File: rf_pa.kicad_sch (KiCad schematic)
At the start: 42 parts, among them Q1 BSS138, Q2 NP100P04PDG, U1 LM317_SOT-223, U2 LT1013DIDR, U3 TL431, U4 RA60H3847H1

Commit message: Add files via upload
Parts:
- added C9: 100u/50V, Capacitor_SMD:CP_Elec_8x10.5, symbol Device:C_Polarized_Small
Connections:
- net GND: now also C9.2
- net RF_PA_VDD: now also C9.1
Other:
- moved on the sheet: R2
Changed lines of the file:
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@@
+    (stroke (width 0) (type default))
+  )
+  (wire (pts (xy 309.88 204.47) (xy 309.88 207.01))
     (stroke (width 0) (type default))
   )
@@
     (stroke (width 0) (type default))
   )
+  (wire (pts (xy 309.88 195.58) (xy 309.88 199.39))
+    (stroke (width 0) (type default))
+  )
   (wire (pts (xy 184.15 116.84) (xy 184.15 114.3))
     (stroke (width 0) (type default))
@@
     (stroke (width 0) (type default))
   )
-  (wire (pts (xy 278.13 200.66) (xy 278.13 205.74))
+  (wire (pts (xy 278.13 200.66) (xy 278.13 207.01))
     (stroke (width 0) (type default))
   )
@@
     (stroke (width 0) (type default))
   )
-  (wire (pts (xy 266.7 195.58) (xy 266.7 198.12))
+  (wire (pts (xy 266.7 195.58) (xy 266.7 199.39))
     (stroke (width 0) (type default))
   )
@@
     (stroke (width 0) (type default))
   )
-  (wire (pts (xy 266.7 203.2) (xy 266.7 205.74))
+  (wire (pts (xy 266.7 204.47) (xy 266.7 207.01))
     (stroke (width 0) (type default))
   )
@@
     )
   )
-  (symbol (lib_id "power:GND") (at 266.7 205.74 0) (unit 1)
-    (in_bom yes) (on_board yes) (dnp no) (fields_autoplaced)
-    (property "Reference" "#PWR015" (at 266.7 212.09 0)
-      (effects (font (size 1.27 1.27)) hide)
-    )
-    (property "Value" "GND" (at 266.7 209.8731 0)
-      (effects (font (size 1.27 1.27)))
-    )
-    (property "Footprint" "" (at 266.7 205.74 0)
-      (effects (font (size 1.27 1.27)) hide)
-    )
-    (property "Datasheet" "" (at 266.7 205.74 0)
+  (symbol (lib_id "power:GND") (at 266.7 207.01 0) (unit 1)
+    (in_bom yes) (on_board yes) (dnp no) (fields_autoplaced)
+    (property "Reference" "#PWR015" (at 266.7 213.36 0)
+      (effects (font (size 1.27 1.27)) hide)
+    )
+    (property "Value" "GND" (at 266.7 211.1431 0)
+      (effects (font (size 1.27 1.27)))
+    )
+    (property "Footprint" "" (at 266.7 207.01 0)
+      (effects (font (size 1.27 1.27)) hide)
+    )
+    (property "Datasheet" "" (at 266.7 207.01 0)
       (effects (font (size 1.27 1.27)) hide)
     )
@@
     )
   )
-  (symbol (lib_id "Device:R_Small") (at 266.7 200.66 180) (unit 1)
+  (symbol (lib_id "Device:R_Small") (at 266.7 201.93 180) (unit 1)
     (in_bom yes) (on_board yes) (dnp no)
-    (property "Reference" "R2" (at 270.51 199.39 0)
-      (effects (font (size 1.27 1.27)))
-    )
-    (property "Value" "10k" (at 270.51 201.93 0)
-      (effects (font (size 1.27 1.27)))
-    )
-    (property "Footprint" "Resistor_SMD:R_0603_1608Metric" (at 266.7 200.66 0)
-      (effects (font (size 1.27 1.27)) hide)
-    )
-    (property "Datasheet" "~" (at 266.7 200.66 0)
-      (effects (font (size 1.27 1.27)) hide)
-    )
-    (property "PN" "" (at 266.7 200.66 0)
+    (property "Reference" "R2" (at 270.51 200.66 0)
+      (effects (font (size 1.27 1.27)))
+    )
+    (property "Value" "10k" (at 270.51 203.2 0)
+      (effects (font (size 1.27 1.27)))
+    )
+    (property "Footprint" "Resistor_SMD:R_0603_1608Metric" (at 266.7 201.93 0)
+      (effects (font (size 1.27 1.27)) hide)
+    )
+    (property "Datasheet" "~" (at 266.7 201.93 0)
+      (effects (font (size 1.27 1.27)) hide)
+    )
+    (property "PN" "" (at 266.7 201.93 0)
       (effects (font (size 1.27 1.27)) hide)
     )
@@
     )
   )
-  (symbol (lib_id "power:GND") (at 278.13 205.74 0) (unit 1)
-    (in_bom yes) (on_board yes) (dnp no) (fields_autoplaced)
-    (property "Reference" "#PWR016" (at 278.13 212.09 0)
-      (effects (font (size 1.27 1.27)) hide)
-    )
-    (property "Value" "GND" (at 278.13 209.8731 0)
-      (effects (font (size 1.27 1.27)))
-    )
-    (property "Footprint" "" (at 278.13 205.74 0)
-      (effects (font (size 1.27 1.27)) hide)
-    )
-    (property "Datasheet" "" (at 278.13 205.74 0)
+  (symbol (lib_id "power:GND") (at 278.13 207.01 0) (unit 1)
+    (in_bom yes) (on_board yes) (dnp no) (fields_autoplaced)
+    (property "Reference" "#PWR016" (at 278.13 213.36 0)
+      (effects (font (size 1.27 1.27)) hide)
+    )
+    (property "Value" "GND" (at 278.13 211.1431 0)
+      (effects (font (size 1.27 1.27)))
+    )
+    (property "Footprint" "" (at 278.13 207.01 0)
+      (effects (font (size 1.27 1.27)) hide)
+    )
+    (property "Datasheet" "" (at 278.13 207.01 0)
       (effects (font (size 1.27 1.27)) hide)
     )
@@
         (path "/4c42207c-9e6b-42da-ad38-da126b892014/7ebe248e-d508-4395-8ad3-4ea02a49e591"
           (reference "U1") (unit 1)
+        )
+      )
+    )
+  )
+  (symbol (lib_id "power:GND") (at 309.88 207.01 0) (unit 1)
+    (in_bom yes) (on_board yes) (dnp no) (fields_autoplaced)
+    (property "Reference" "#PWR018" (at 309.88 213.36 0)
+      (effects (font (size 1.27 1.27)) hide)
+    )
+    (property "Value" "GND" (at 309.88 211.1431 0)
+      (effects (font (size 1.27 1.27)))
+    )
+    (property "Footprint" "" (at 309.88 207.01 0)
+      (effects (font (size 1.27 1.27)) hide)
+    )
+    (property "Datasheet" "" (at 309.88 207.01 0)
+      (effects (font (size 1.27 1.27)) hide)
+    )
+    (pin "1")
+    (instances
+      (project "m17-rru-rf"
+        (path "/4c42207c-9e6b-42da-ad38-da126b892014/7ebe248e-d508-4395-8ad3-4ea02a49e591"
+          (reference "#PWR018") (unit 1)
         )
       )
@@
         )
       )
+    )
+  )
+  (symbol (lib_id "Device:C_Polarized_Small") (at 309.88 201.93 0) (unit 1)
+    (in_bom yes) (on_board yes) (dnp no) (fields_autoplaced)
+    (property "Reference" "C9" (at 312.039 200.1718 0)
+      (effects (font (size 1.27 1.27)) (justify left))
+    )
+    (property "Value" "100u/50V" (at 312.039 202.596 0)
+      (effects (font (size 1.27 1.27)) (justify left))
+    )
+    (property "Footprint" "Capacitor_SMD:CP_Elec_8x10.5" (at 309.88 201.93 0)
+      (effects (font (size 1.27 1.27)) hide)
+    )
+    (property "Datasheet" "~" (at 309.88 201.93 0)
+      (effects (font (size 1.27 1.27)) hide)
+    )
+    (property "PN" "50SEV100M8X10.5" (at 309.88 201.93 0)
+      (effects (font (size 1.27 1.27)) hide)
+    )
+    (pin "1")
+    (pin "2")
+    (instances
+      (project "m17-rru-rf"
+        (path "/4c42207c-9e6b-42da-ad38-da126b892014/7ebe248e-d508-4395-8ad3-4ea02a49e591"
+          (reference "C9") (unit 1)
+        )
+      )

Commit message: Add files via upload
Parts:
- added Q1: BSS138, Package_TO_SOT_SMD:SOT-23, symbol Transistor_FET:BSS138
- added R2: 100k, Resistor_SMD:R_0603_1608Metric, symbol Device:R_Small
- added R2: 100R, Resistor_SMD:R_0603_1608Metric, symbol Device:R_Small
- added R2: 10k, Resistor_SMD:R_0603_1608Metric, symbol Device:R_Small
- added TP5: ~, TestPoint:TestPoint_Pad_D1.5mm, symbol Connector:TestPoint_Probe
- Q2: renamed from Q1; PN (none) -> BSS138P,215
- R2: value 47k -> 12k
- renumbered Q2 to Q3, TP5 to TP6, TP6 to TP7
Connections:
- net at Q2.1 (G), R2.2, R2.2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: now also R2.1
- net at Q3.1 (G), R2.1, TP7.1: now also Q1.3 (D); no longer Q2.3 (D)
- net PA_EN renamed PA_EN_B
- new net: Q1.2 (S), Q2.3 (D), R2.1, R2.2
- new net: Q1.1 (G), R2.2, R2.2, TP5.1
- new net PA_EN_A: R2.1
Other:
- moved on the sheet: C9, D3, D4, Q2, Q3, R2, TP6, TP7

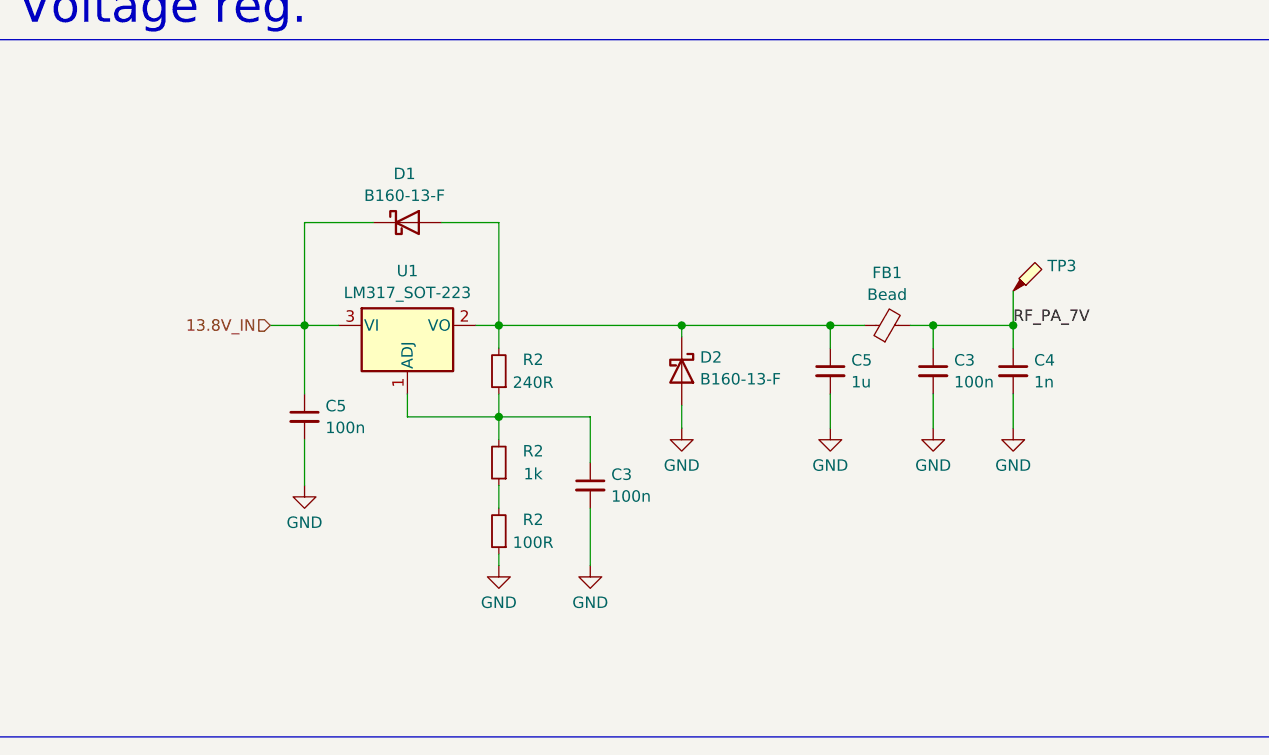
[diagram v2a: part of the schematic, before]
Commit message: LM317 protection diode location update
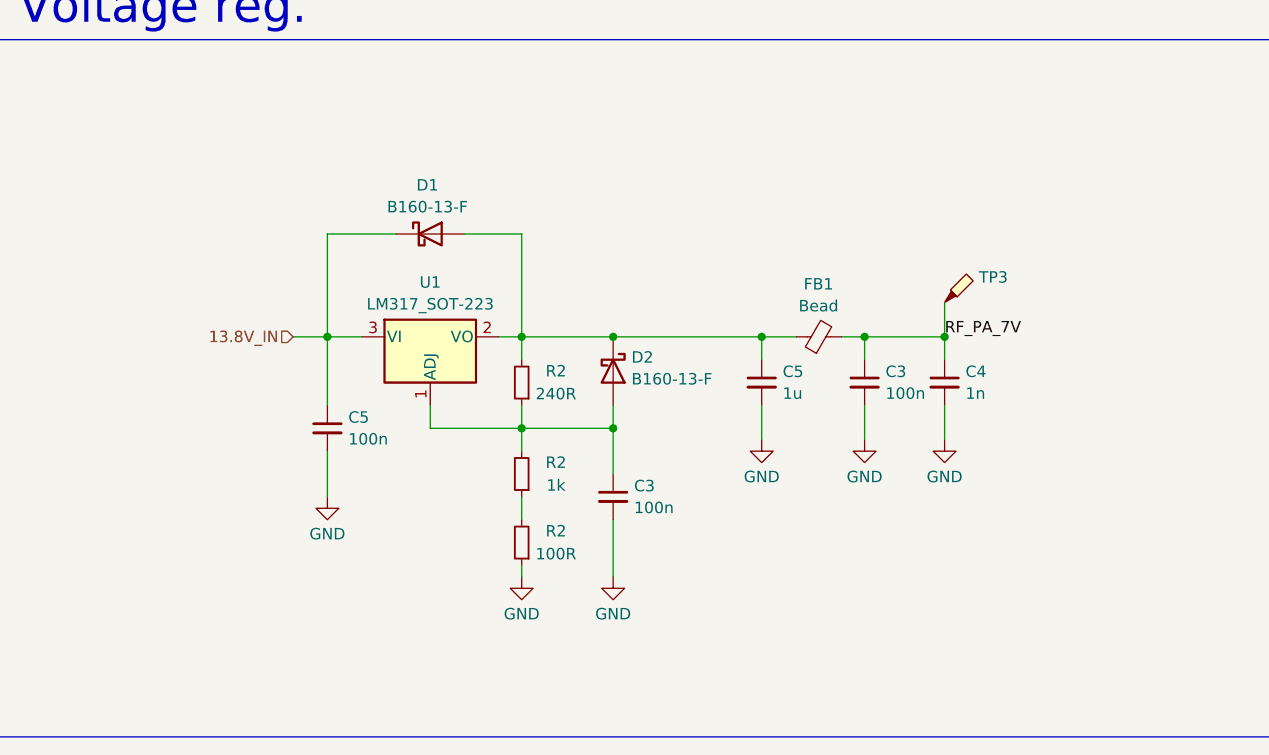
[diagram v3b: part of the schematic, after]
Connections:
- net GND: no longer D2.2 (A)
- net at C3.1, R2.1, R2.2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: now also D2.2 (A)
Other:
- moved on the sheet: C3, C4, C5, D1, D2, FB1, R2, TP3, U1

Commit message: partial PN update
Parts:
- added C3: 3n9, Capacitor_SMD:C_0603_1608Metric, symbol Device:C_Small
- added TP1, TP2: ~, TestPoint:TestPoint_Pad_D1.5mm, symbol Connector:TestPoint_Probe
- C3, C5: PN (none) -> C0603C104M5RAC7411
- C3: PN (none) -> GCM1885C1H392JA16J
- C4: PN (none) -> C0603C102J5GAC7411
- C5: PN (none) -> CL10B105KB8NQNC
- renumbered C9 to C10, TP1 to TP3, TP2 to TP4, TP3 to TP5, TP4 to TP6, TP5 to TP7, TP6 to TP8, TP7 to TP9
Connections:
- net FWD_SENSE_IN: now also TP1.1
- net at R2.1, R2.2, R2.2: now also TP2.1
- net at R2.1, R2.1, U2.4 (2IN-): now also C3.2
- net at R2.2, U2.5 (2OUT): now also C3.1
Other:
- moved on the sheet: D2

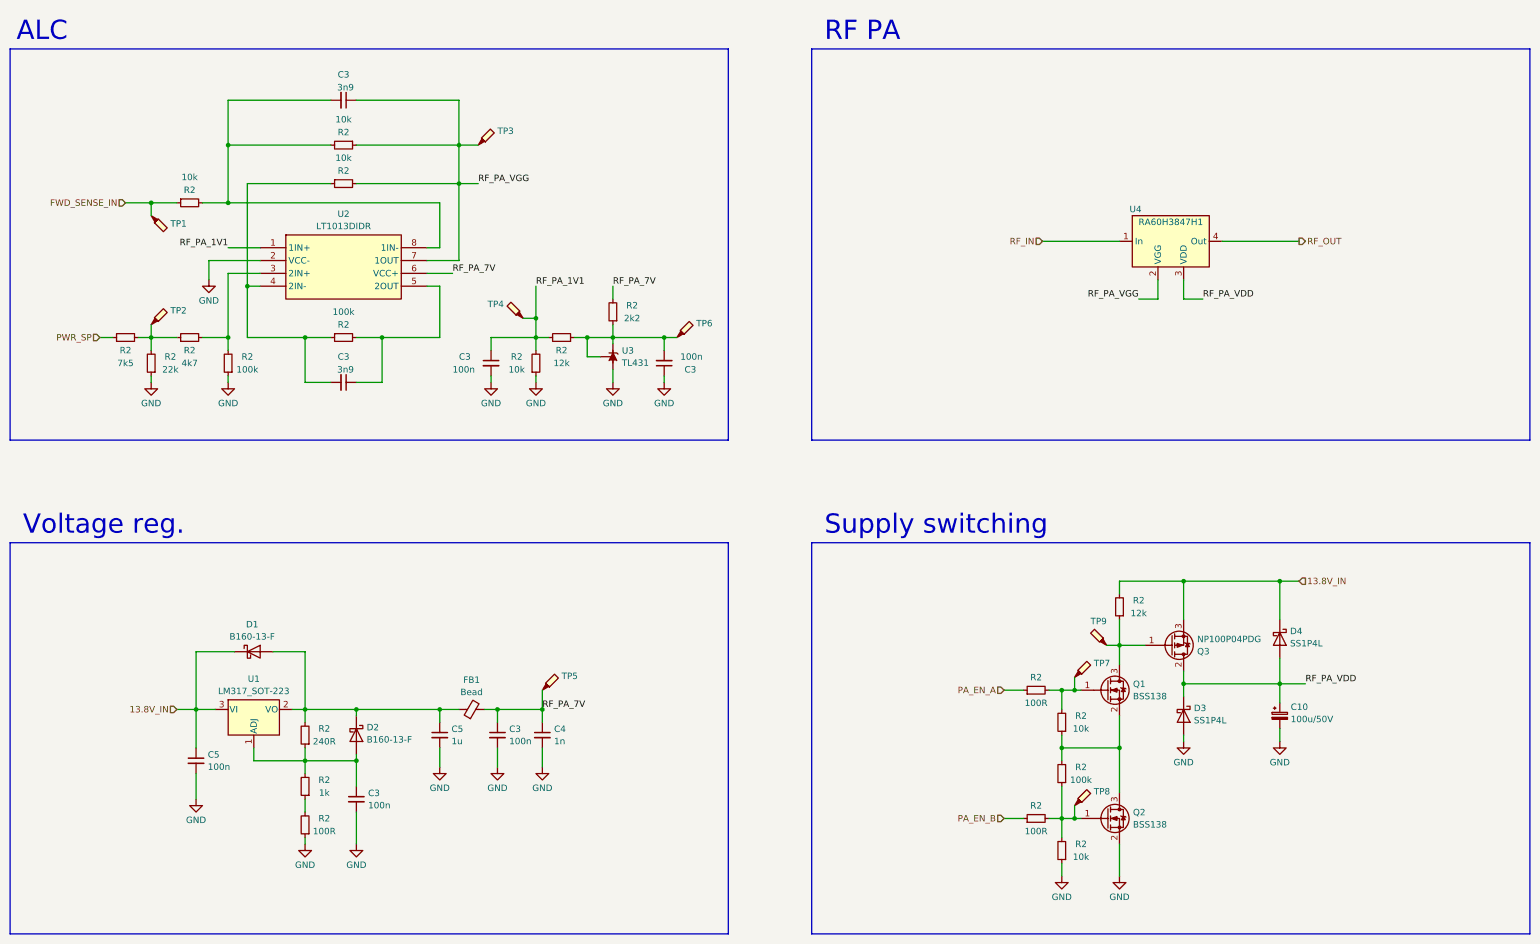
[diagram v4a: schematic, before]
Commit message: RF PA's Vgg signal fix
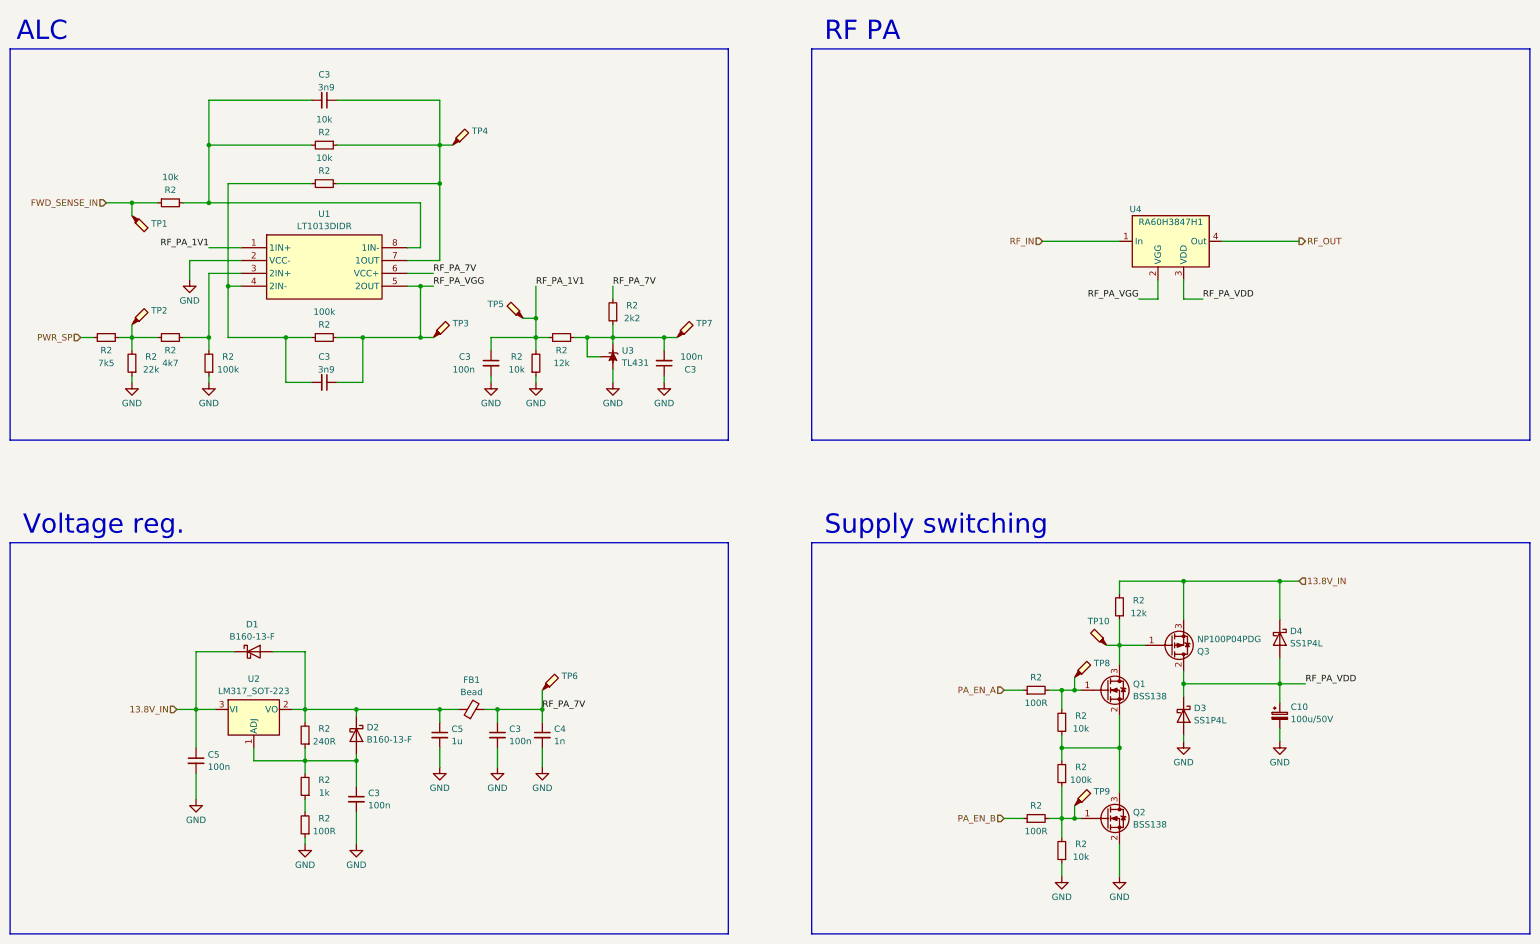
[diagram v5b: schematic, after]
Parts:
- added TP3: ~, TestPoint:TestPoint_Pad_D1.5mm, symbol Connector:TestPoint_Probe
- renumbered TP9 to TP10, TP3 to TP4, TP4 to TP5, TP5 to TP6, TP6 to TP7, TP7 to TP8, TP8 to TP9, U2 to U1, U1 to U2
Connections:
- net RF_PA_VGG: now also C3.1, R2.2, U1.5 (2OUT), TP3.1; no longer C3.1, R2.1, R2.2, TP4.1, U1.7 (1OUT)
- new net: C3.1, R2.1, R2.2, TP4.1, U1.7 (1OUT)
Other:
- moved on the sheet: C3, R2, TP1, TP2, TP4, U1

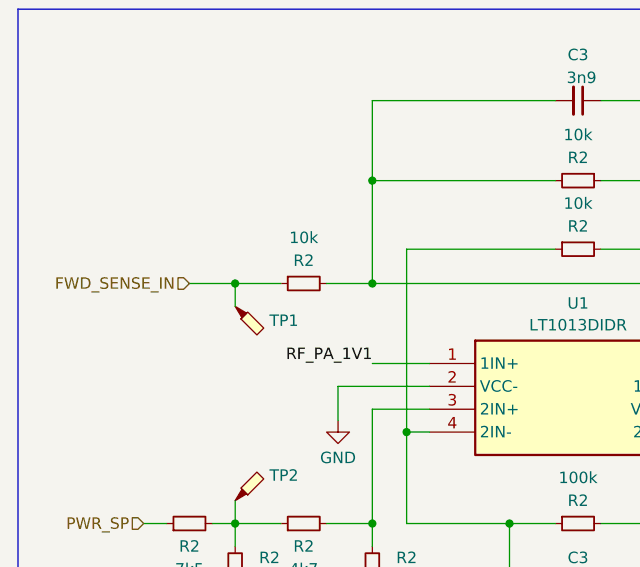
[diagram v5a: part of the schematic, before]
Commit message: significant updates
- supply for the detector block changed from 3.3V to 5V
- minor bugfixes
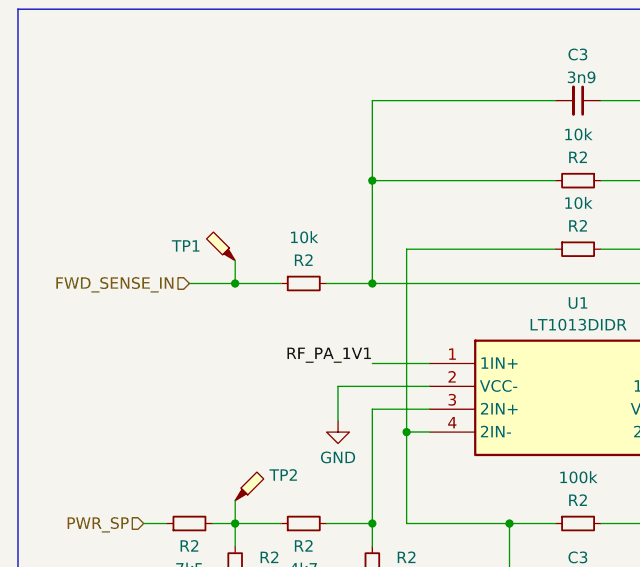
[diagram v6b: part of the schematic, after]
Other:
- moved on the sheet: TP1
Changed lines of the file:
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@@
-    (stroke (width 0) (type default))
-  )
-  (wire (pts (xy 78.74 87.63) (xy 78.74 90.17))
     (stroke (width 0) (type default))
   )
@@
   )
   (wire (pts (xy 133.35 101.6) (xy 138.43 101.6))
+    (stroke (width 0) (type default))
+  )
+  (wire (pts (xy 78.74 85.09) (xy 78.74 87.63))
     (stroke (width 0) (type default))
   )
@@
     )
   )
-  (symbol (lib_id "Connector:TestPoint_Probe") (at 78.74 90.17 270) (unit 1)
-    (in_bom yes) (on_board yes) (dnp no) (fields_autoplaced)
-    (property "Reference" "TP1" (at 82.55 91.7575 90)
-      (effects (font (size 1.27 1.27)) (justify left))
-    )
-    (property "Value" "~" (at 79.1154 93.98 0)
-      (effects (font (size 1.27 1.27)) (justify left))
-    )
-    (property "Footprint" "TestPoint:TestPoint_Pad_D1.5mm" (at 78.74 95.25 0)
-      (effects (font (size 1.27 1.27)) hide)
-    )
-    (property "Datasheet" "~" (at 78.74 95.25 0)
-      (effects (font (size 1.27 1.27)) hide)
-    )
+  (symbol (lib_id "Connector:TestPoint_Probe") (at 78.74 85.09 90) (unit 1)
+    (in_bom yes) (on_board yes) (dnp no)
+    (property "Reference" "TP1" (at 74.93 83.5025 90)
+      (effects (font (size 1.27 1.27)) (justify left))
+    )
+    (property "Value" "~" (at 78.3646 81.28 0)
+      (effects (font (size 1.27 1.27)) (justify left))
+    )
+    (property "Footprint" "TestPoint:TestPoint_Pad_D1.5mm" (at 78.74 80.01 0)
+      (effects (font (size 1.27 1.27)) hide)
+    )
+    (property "Datasheet" "~" (at 78.74 80.01 0)
+      (effects (font (size 1.27 1.27)) hide)
+    )
